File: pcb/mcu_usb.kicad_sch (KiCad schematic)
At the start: 33 parts, among them J12 USB_C_Receptacle, J13 UPDI, U10 CP2102N-A02-GQFN24, U11 TLV75533PDBV, U9 AVR128DA48-E/PT, Y1 32.768kHz

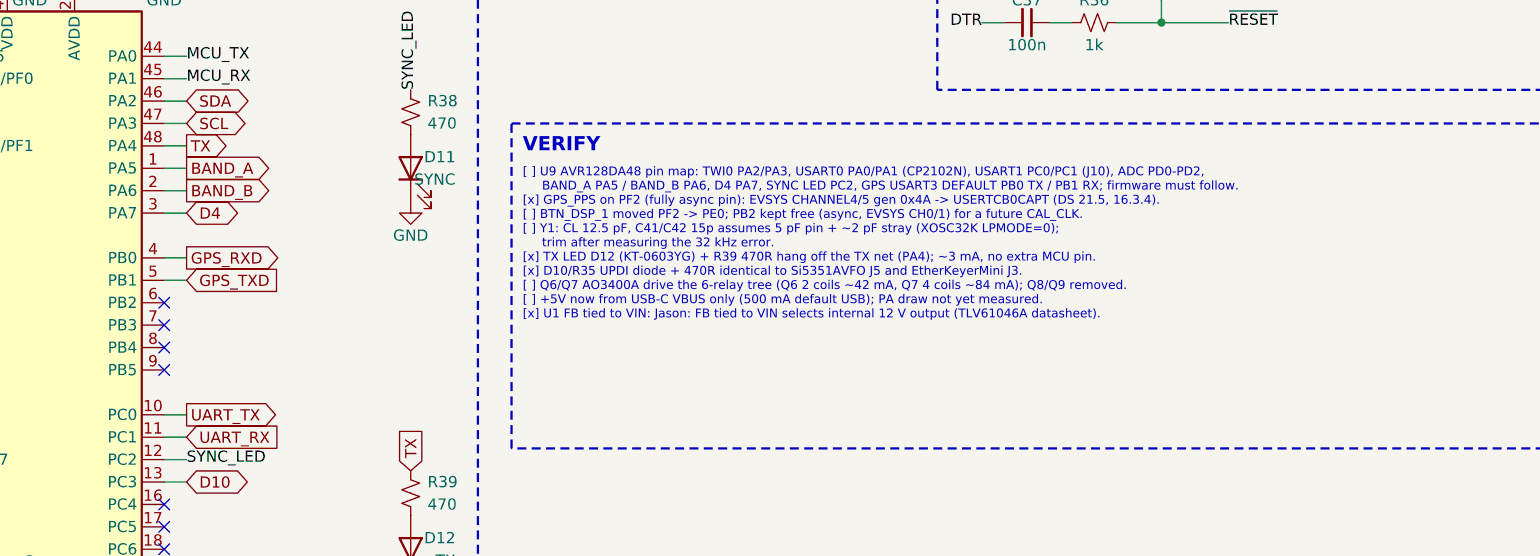
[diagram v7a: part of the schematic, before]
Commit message: Replace Si5351A with Si5351C; add SMA CLKIN and CAL_CLK to PB2
- U4 SI5351C-B-GMR (LCSC C2649375, alt SI5351C-B-GM C3608122), QFN-20 4x4 EP2.7, EP to GND
- TCXO stays on XA (XB open); CLK0 to PA buffer and CLK2 to J6 unchanged
- J16 BWSMA-KE-P001 (C496550) to CLKIN: 49.9R term, 100n AC coupling, 10k/10k VDD/2 bias
- CLK4 -> R47 33R -> CAL_CLK -> PB2 (EVSYS CH0/1); PPS stays on PF2 (CH4/5)
- OEB tied low; INTR 10k pull-up -> SI_INTR -> PB3
- 100n on VDD and each VDDOx (C14, C50-C53)
- VERIFY: Si5351C section, 10 s PPS-gated 32-bit TCB0/TCB1 cascade count
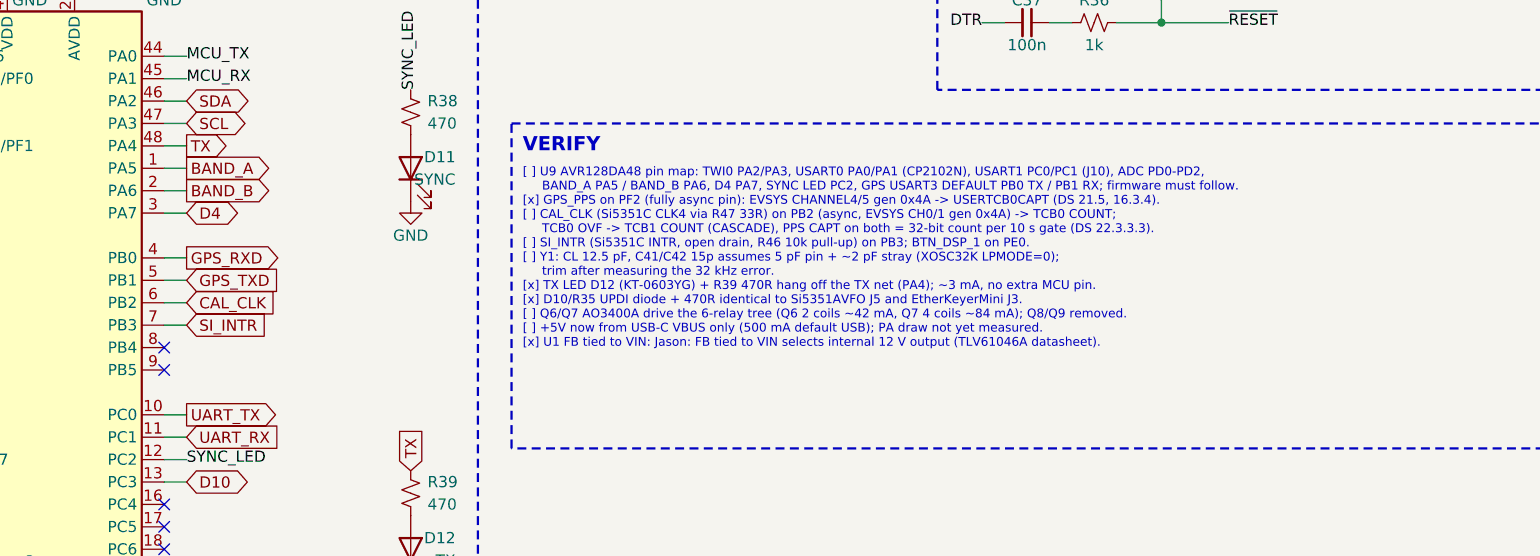
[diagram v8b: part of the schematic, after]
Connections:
- net CAL_CLK: now reaches U9.6 (PB2)
- net SI_INTR: now reaches U9.7 (PB3)
- no-connect marks 29 -> 27
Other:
- note added: "[ ] U9 AVR128DA48 pin map: TWI0 PA2/PA3, USART0 PA0/PA1 (CP2102N), USART1 PC0/PC1 (J10), ADC PD0-PD2, BAND_A PA5 / BAND_B PA6, D4 PA7, SYNC LED PC2, GPS USART3 DEFAULT PB0 TX / PB1 RX; firmware must follow. [x] GPS_PPS on PF2 (fully async pin): EVSYS CHANNEL4/5 gen 0x4A -> USERTCB0CAPT (DS 21.5, 16.3.4). [ ] CAL_CLK (Si5351C CLK4 via R47 33R) on PB2 (async, EVSYS CH0/1 gen 0x4A) -> TCB0 COUNT; TC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"
- note removed: "[ ] U9 AVR128DA48 pin map: TWI0 PA2/PA3, USART0 PA0/PA1 (CP2102N), USART1 PC0/PC1 (J10), ADC PD0-PD2, BAND_A PA5 / BAND_B PA6, D4 PA7, SYNC LED PC2, GPS USART3 DEFAULT PB0 TX / PB1 RX; firmware must follow. [x] GPS_PPS on PF2 (fully async pin): EVSYS CHANNEL4/5 gen 0x4A -> USERTCB0CAPT (DS 21.5, 16.3.4). [ ] BTN_DSP_1 moved PF2 -> PE0; PB2 kept free (async, EVSYS CH0/1) for a future CAL_CLK. [ ] 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"
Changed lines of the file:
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@@
-	)
-	(no_connect
-		(at 111.76 148.59)
-	)
-	(no_connect
-		(at 111.76 151.13)
 	)
 	(no_connect
@@
 		(property "Intersheetrefs" "${INTERSHEET_REFS}"
 			(at 114.3 168.91 0)
+			(effects
+				(font
+					(size 1.27 1.27)
+				)
+				(hide yes)
+			)
+		)
+	)
+	(wire
+		(pts
+			(xy 111.76 148.59)
+			(xy 114.3 148.59)
+		)
+		(stroke
+			(width 0)
+			(type default)
+		)
+	)
+	(global_label "CAL_CLK"
+		(shape input)
+		(at 114.3 148.59 0)
+		(fields_autoplaced yes)
+		(effects
+			(font
+				(size 1.27 1.27)
+				(color 0 120 120 1)
+			)
+			(justify left)
+		)
+		(property "Intersheetrefs" "${INTERSHEET_REFS}"
+			(at 114.3 148.59 0)
+			(effects
+				(font
+					(size 1.27 1.27)
+				)
+				(hide yes)
+			)
+		)
+	)
+	(wire
+		(pts
+			(xy 111.76 151.13)
+			(xy 114.3 151.13)
+		)
+		(stroke
+			(width 0)
+			(type default)
+		)
+	)
+	(global_label "SI_INTR"
+		(shape input)
+		(at 114.3 151.13 0)
+		(fields_autoplaced yes)
+		(effects
+			(font
+				(size 1.27 1.27)
+				(color 0 120 120 1)
+			)
+			(justify left)
+		)
+		(property "Intersheetrefs" "${INTERSHEET_REFS}"
+			(at 114.3 151.13 0)
 			(effects
 				(font
@@
 		)
 	)
-	(text "[ ] U9 AVR128DA48 pin map: TWI0 PA2/PA3, USART0 PA0/PA1 (CP2102N), USART1 PC0/PC1 (J10), ADC PD0-PD2,\n     BAND_A PA5 / BAND_B PA6, D4 PA7, SYNC LED PC2, GPS USART3 DEFAULT PB0 TX / PB1 RX; firmware must follow.\n[x] GPS_PPS on PF2 (fully async pin): EVSYS CHANNEL4/5 gen 0x4A -> USERTCB0CAPT (DS 21.5, 16.3.4).\n[ ] BTN_DSP_1 moved PF2 -> PE0; PB2 kept free (async, EVSYS CH0/1) for a future CAL_CLK.\n[ ] Y1: CL 12.5 pF, C41/C42 15p assumes 5 pF pin + ~2 pF stray (XOSC32K LPMODE=0);\n     trim after measuring the 32 kHz error.\n[x] TX LED D12 (KT-0603YG) + R39 470R hang off the TX net (PA4); ~3 mA, no extra MCU pin.\n[x] D10/R35 UPDI diode + 470R identical to Si5351AVFO J5 and EtherKeyerMini J3.\n[ ] Q6/Q7 AO3400A drive the 6-relay tree (Q6 2 coils ~42 mA, Q7 4 coils ~84 mA); Q8/Q9 removed.\n[ ] +5V now from USB-C VBUS only (500 mA default USB); PA draw not yet measured.\n[x] U1 FB tied to VIN: Jason: FB tied to VIN selects internal 12 V output (TLV61046A datasheet)."
+	(text "[ ] U9 AVR128DA48 pin map: TWI0 PA2/PA3, USART0 PA0/PA1 (CP2102N), USART1 PC0/PC1 (J10), ADC PD0-PD2,\n     BAND_A PA5 / BAND_B PA6, D4 PA7, SYNC LED PC2, GPS USART3 DEFAULT PB0 TX / PB1 RX; firmware must follow.\n[x] GPS_PPS on PF2 (fully async pin): EVSYS CHANNEL4/5 gen 0x4A -> USERTCB0CAPT (DS 21.5, 16.3.4).\n[ ] CAL_CLK (Si5351C CLK4 via R47 33R) on PB2 (async, EVSYS CH0/1 gen 0x4A) -> TCB0 COUNT;\n     TCB0 OVF -> TCB1 COUNT (CASCADE), PPS CAPT on both = 32-bit count per 10 s gate (DS 22.3.3.3).\n[ ] SI_INTR (Si5351C INTR, open drain, R46 10k pull-up) on PB3; BTN_DSP_1 on PE0.\n[ ] Y1: CL 12.5 pF, C41/C42 15p assumes 5 pF pin + ~2 pF stray (XOSC32K LPMODE=0);\n     trim after measuring the 32 kHz error.\n[x] TX LED D12 (KT-0603YG) + R39 470R hang off the TX net (PA4); ~3 mA, no extra MCU pin.\n[x] D10/R35 UPDI diode + 470R identical to Si5351AVFO J5 and EtherKeyerMini J3.\n[ ] Q6/Q7 AO3400A drive the 6-relay tree (Q6 2 coils ~42 mA, Q7 4 coils ~84 mA); Q8/Q9 removed.\n[ ] +5V now from USB-C VBUS only (500 mA default USB); PA draw not yet measured.\n[x] U1 FB tied to VIN: Jason: FB tied to VIN selects internal 12 V output (TLV61046A datasheet)."
 		(exclude_from_sim no)
 		(at 152.4 133.35 0)
